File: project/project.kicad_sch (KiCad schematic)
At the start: 33 parts, among them J1 ssd1306 oled, SW1 USR_BTN, T1 xh3p, T2 xh3p, T3 xh3p, T4 xh3p, T5 xh3p, T6 xh3p, T7 xh3p, T8 xh3p, U1 esp32-c3-supermini

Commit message: everything has changed
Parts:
- removed R15: 330, Resistor_SMD:R_0805_2012Metric, symbol Device:R
- removed R16: 4k7, Resistor_SMD:R_0805_2012Metric, symbol Device:R
- removed T1, T2, T3, T4, T5, T6, T7, T8: xh3p, -local:JST_XH_S3B-XH-SM4-TB_1x03-1MP_P2.50mm_Horizontal, symbol Connector_Generic_MountingPin:Conn_01x03_MountingPin
- added C1: 10u, Capacitor_SMD:C_0805_2012Metric_Pad1.18x1.45mm_HandSolder, symbol Device:C
- added D2: LED, LED_SMD:LED_0805_2012Metric_Pad1.15x1.40mm_HandSolder, symbol Device:LED
- added R18, R21, R22, R3: 330, Resistor_SMD:R_0805_2012Metric, symbol Device:R
- added R19, R2, R20: 4k7, Resistor_SMD:R_0805_2012Metric, symbol Device:R
- added SW1: USR_BTN, Button_Switch_SMD:SW_SPST_PTS645, symbol Switch:SW_Push
- added T1, T2, T3, T4, T5, T6, T7, T8: PJ-242, -local:PJ-242, symbol Connector:AudioJack4_SwitchTR1
- J1: footprint -local:oled_i2c_128x32_ssd1306 -> -local:oled_i2c_128x64_ssd1306
- R1, R10, R11, R12, R13, R14, R17, R4, R5, R6, R7, R8, R9: lcsc# C17414 -> (none)
- R15: renamed from R3; lcsc# C17414 -> (none)
- R16: renamed from R2; lcsc# C17414 -> (none)
- renumbered C1 to C2, SW1 to SW2
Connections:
- net +3V3: now also R1.2, R10.2, R11.2, R12.2, R13.2, R14.2, R15.2, R16.2, R4.2, R5.2, R6.2, R7.2, R8.2, R9.2, C1.1, R19.2, R2.2, R20.2, R3.2; no longer R10.1, R11.1, R12.1, R13.1, R14.1, R15.1, R16.1, R17.1, R4.1, R5.1, R6.1, R7.1, R8.1, R9.1
- net GND: now also C1.2, D2.1 (K), SW1.2, T1.R2, T2.R2, T3.R2, T4.R2, T5.R2, T6.R2, T7.R2, T8.R2
- net LED: now also R17.2, R18.2; no longer R1.1
- net SCL: now also R20.1
- net SDA: now also R19.1
- net T1: now also U1.13 (IO4/ADC1_4/SPI_SCK), R2.1, T1.T; no longer R16.2, U1.1 (IO5/ADC2/SPI_MISO)
- net T2: now also R4.1, U1.12 (IO3/ADC1_3), T2.T; no longer R4.2, U1.6 (IO10)
- net T3: now also R6.1, U1.10 (IO1/ADC1_1), T3.T; no longer R6.2, U1.2 (IO6/SPI_MOSI)
- net T4: now also R8.1, U1.9 (IO0/ADC1_0), T4.T; no longer R8.2, U1.3 (IO7/SPI_SS)
- net T5: now also R10.1, U1.1 (IO5/ADC2/SPI_MISO), T5.T; no longer R10.2, U1.12 (IO3/ADC1_3)
- net T6: now also R12.1, U1.2 (IO6/SPI_MOSI), T6.T; no longer R12.2, U1.10 (IO1/ADC1_1)
- net T7: now also R14.1, U1.3 (IO7/SPI_SS), T7.T; no longer R14.2, U1.9 (IO0/ADC1_0)
- net T8: now also R16.1, U1.6 (IO10), T8.T; no longer U1.13 (IO4/ADC1_4/SPI_SCK)
- net BTN2: now reaches U1.8 (IO21/TX)
- net BTN2: now also R22.1
- net at D1.1 (K): now also R17.1; no longer R1.2
- net BTN: no longer names the net of SW2.1
- net BTN: now also R22.2; no longer U1.11 (IO2/ADC1_2/BOOT)
- new net: R3.1, T2.S
- new net: R1.1, T1.S
- new net: R13.1, T7.S
- new net: R9.1, T5.S
- new net: D2.2 (A), R18.1
- new net: R21.2, SW1.1
- new net: R5.1, T3.S
- new net: R7.1, T4.S
- new net: R15.1, T8.S
- new net: R11.1, T6.S
- new net BTN1: R21.1, U1.11 (IO2/ADC1_2/BOOT)
- no-connect marks 1 -> 24
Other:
- moved on the sheet: C2, D1, J1, R15, R16, SW2, U1

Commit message: updating bom and pnp positions
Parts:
- C1, C2: jlc-part-type (none) -> B; lcsc# (none) -> C15850
- D1: value LED -> LED-R; jlc-part-type (none) -> B; lcsc# (none) -> C84256
- D2: value LED -> LED-G; jlc-part-type (none) -> B; lcsc# (none) -> C2297
- H1, J1, U1: jlc-part-type (none) -> -
- R1, R11, R13, R15, R17, R18, R21, R22, R3, R5, R7, R9: lcsc# (none) -> C17630
- R10, R12, R14, R16, R19, R2, R20, R4, R6, R8: lcsc# (none) -> C17673
- SW1, SW2: jlc-part-type (none) -> E; lcsc# (none) -> C2689405
- T1, T2, T3, T4, T5, T6, T7, T8: jlc-part-type (none) -> E

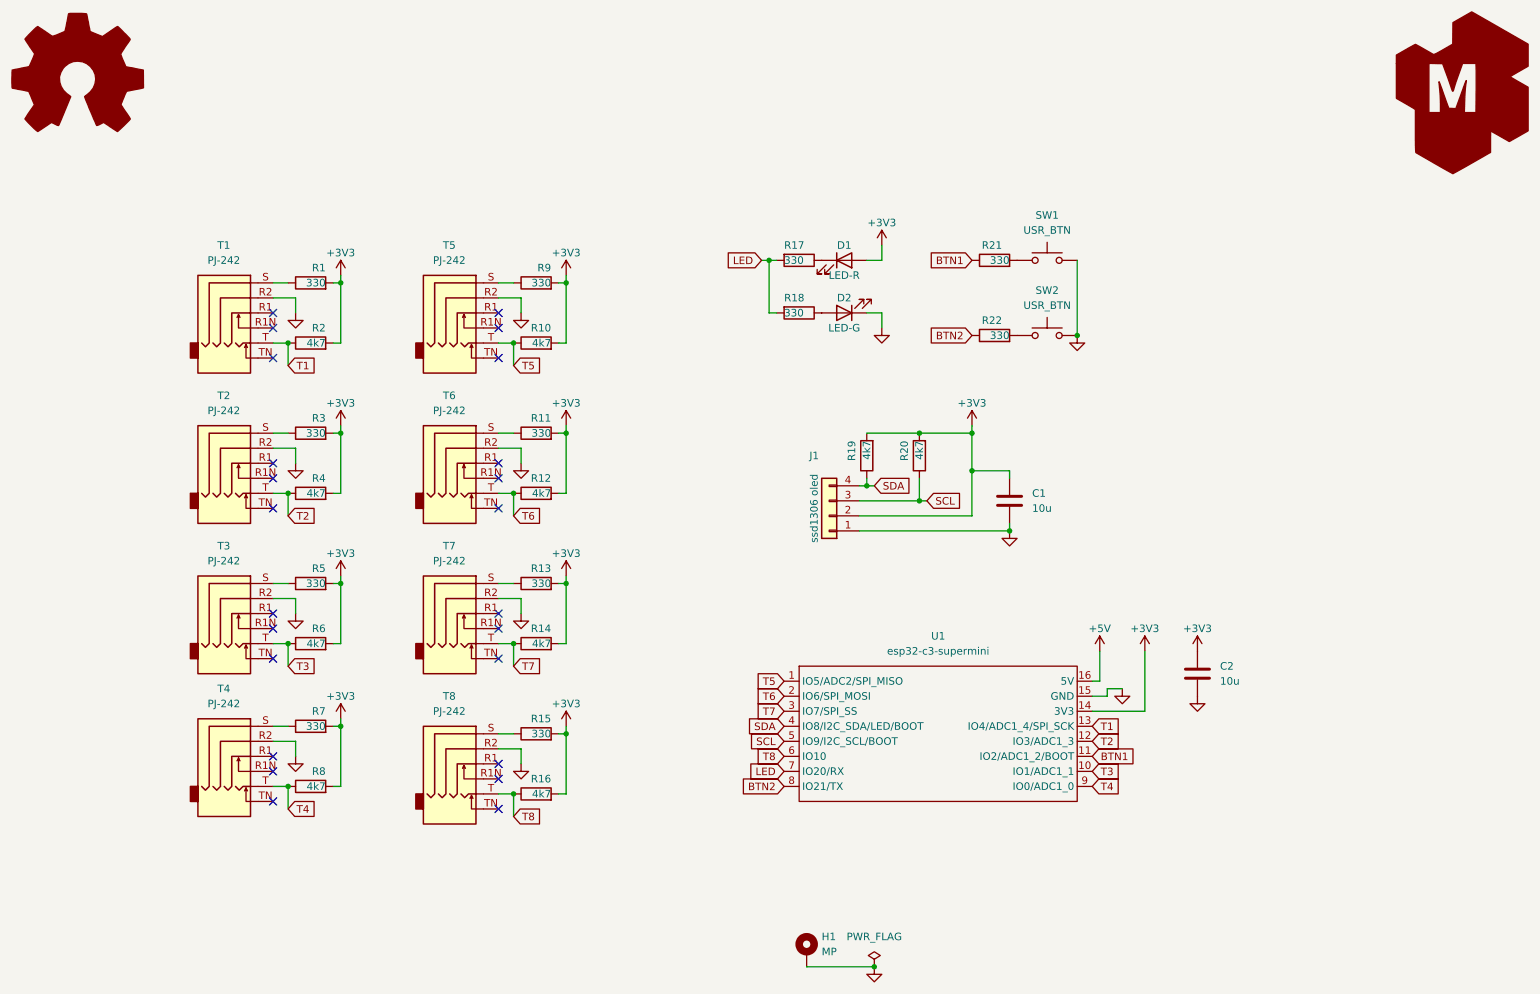
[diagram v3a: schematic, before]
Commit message: fixed bugs from v1.0
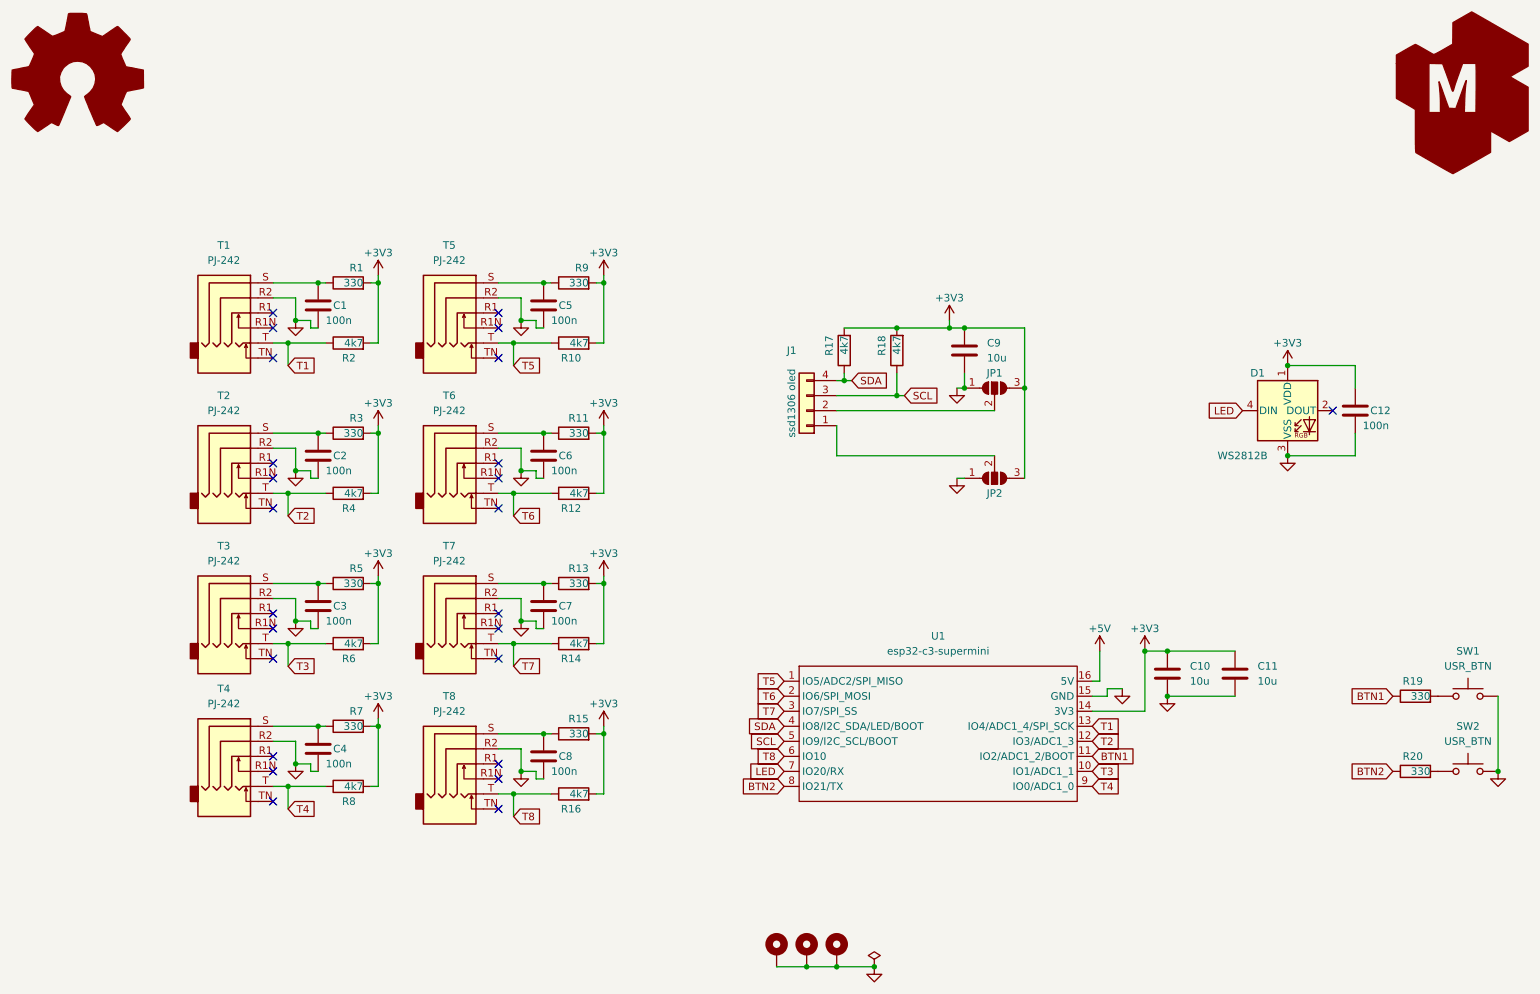
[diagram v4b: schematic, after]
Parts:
- removed D1: LED-R, LED_SMD:LED_0805_2012Metric_Pad1.15x1.40mm_HandSolder, symbol Device:LED
- removed D2: LED-G, LED_SMD:LED_0805_2012Metric_Pad1.15x1.40mm_HandSolder, symbol Device:LED
- removed R17, R18: 330, Resistor_SMD:R_0805_2012Metric, symbol Device:R
- added C11, C9: 10u, Capacitor_SMD:C_0805_2012Metric_Pad1.18x1.45mm_HandSolder, symbol Device:C
- added C12, C2, C3, C4, C5, C6, C7, C8: 100n, Capacitor_SMD:C_0805_2012Metric_Pad1.18x1.45mm_HandSolder, symbol Device:C
- added D1: WS2812B, LED_SMD:LED_WS2812B_PLCC4_5.0x5.0mm_P3.2mm, symbol LED:WS2812B
- added H1, H3: MP, MountingHole:MountingHole_3.2mm_M3_DIN965_Pad, symbol Mechanical:MountingHole_Pad
- added JP1: PIN2, Jumper:SolderJumper-3_P1.3mm_Open_RoundedPad1.0x1.5mm, symbol Jumper:SolderJumper_3_Open
- added JP2: PIN1, Jumper:SolderJumper-3_P1.3mm_Open_RoundedPad1.0x1.5mm, symbol Jumper:SolderJumper_3_Open
- C1: value 10u -> 100n; lcsc# C15850 -> C28233
- G1, G2: now in the parts list
- J1: footprint -local:oled_i2c_128x64_ssd1306 -> -local:oled_i2c_1.3_128x64_ssd1306
- renumbered C2 to C10, H1 to H2, R19 to R17, R20 to R18, R21 to R19, R22 to R20
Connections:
- net +3V3: now also C11.1, C12.1, C9.1, D1.1 (VDD), JP1.3 (B), JP2.3 (B); no longer C1.1, J1.2 (Pin_2)
- net GND: now also C11.2, C12.2, C2.2, C3.2, C4.2, C5.2, C6.2, C7.2, C8.2, C9.2, D1.3 (VSS), H1.1, H3.1, JP1.1 (A), JP2.1 (A); no longer J1.1 (Pin_1)
- net LED: now also D1.4 (DIN)
- net at R3.1, T2.S: now also C2.1
- net at R1.1, T1.S: now also C1.1
- net at R13.1, T7.S: now also C7.1
- net at R9.1, T5.S: now also C5.1
- net at R5.1, T3.S: now also C3.1
- net at R7.1, T4.S: now also C4.1
- net at R15.1, T8.S: now also C8.1
- net at R11.1, T6.S: now also C6.1
- new net: J1.2 (Pin_2), JP1.2 (C)
- new net: J1.1 (Pin_1), JP2.2 (C)
- no-connect marks 24 -> 25
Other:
- moved on the sheet: C10, J1, R1, R10, R11, R12, R13, R14, R15, R16, R17, R18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

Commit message: adding hard reset for sensors, removing rgb led
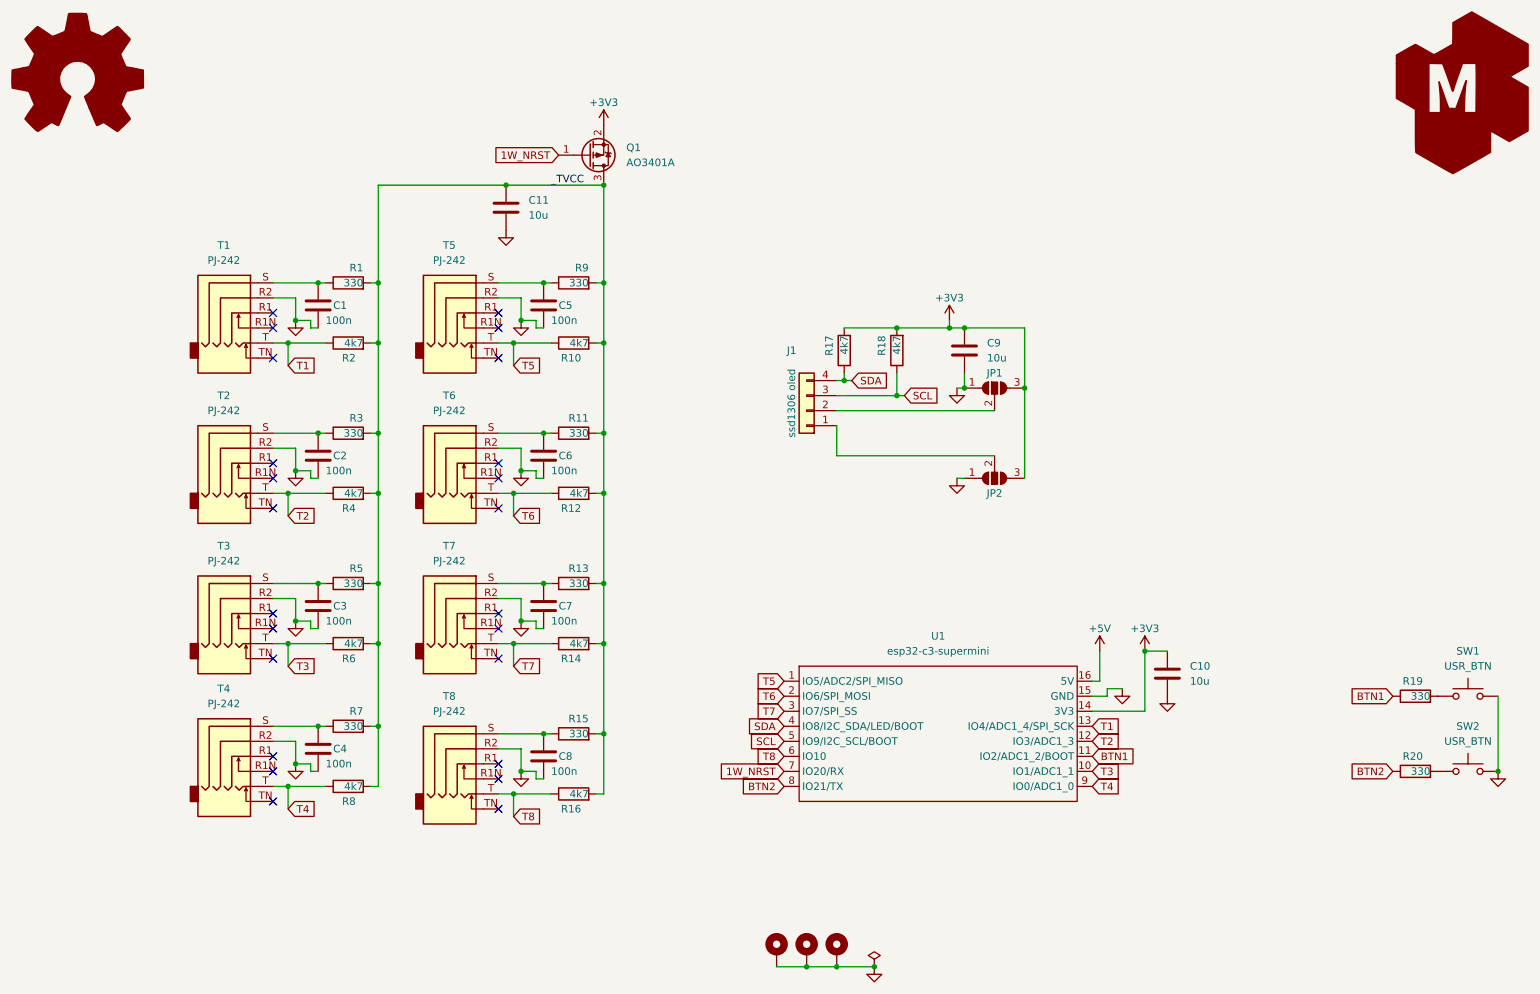
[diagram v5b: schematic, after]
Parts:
- removed C12: 100n, Capacitor_SMD:C_0805_2012Metric_Pad1.18x1.45mm_HandSolder, symbol Device:C
- removed D1: WS2812B, LED_SMD:LED_WS2812B_PLCC4_5.0x5.0mm_P3.2mm, symbol LED:WS2812B
- added Q1: AO3401A, Package_TO_SOT_SMD:SOT-23, symbol Transistor_FET:AO3401A
- G1, G2, JP1: now left out of the parts list
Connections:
- net +3V3: now also Q1.2 (S); no longer C11.1, R1.2, R10.2, R11.2, R12.2, R13.2, R14.2, R15.2, R16.2, R2.2, R3.2, R4.2, R5.2, R6.2, R7.2, R8.2, R9.2
- net LED renamed 1W_NRST
- net 1W_NRST: now also Q1.1 (G)
- new net _TVCC: C11.1, Q1.3 (D), R1.2, R10.2, R11.2, R12.2, R13.2, R14.2, R15.2, R16.2, R2.2, R3.2, R4.2, R5.2, R6.2, R7.2, R8.2, R9.2
- no-connect marks 25 -> 24
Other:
- moved on the sheet: C11

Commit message: numbering inputs, changing buttons, and adding tooling holes
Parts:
- SW1, SW2: footprint Button_Switch_SMD:SW_SPST_PTS645 -> Button_Switch_SMD:SW_SPST_TL3342; jlc-part-type E -> B; lcsc# C2689405 -> C318884
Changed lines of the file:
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@@
   (title_block
     (title "temp-1w8-pro")
-    (date "2024-12-01")
-    (rev "3.0")
+    (date "2024-12-23")
+    (rev "3.1")
     (company "makerspace.lt")
   )
@@
     (property "Reference" "SW1" (id 0) (at 265.43 127 0))
     (property "Value" "USR_BTN" (id 1) (at 265.43 129.54 0))
-    (property "Footprint" "Button_Switch_SMD:SW_SPST_PTS645" (id 2) (at 265.43 129.54 0)
-      (effects (font (size 1.27 1.27)) hide)
-    )
-    (property "Datasheet" "https://wmsc.lcsc.com/wmsc/upload/file/pdf/v2/lcsc/2102191506_DGBZ-YTSD003A0452502B_C2689405.pdf" (id 3) (at 265.43 129.54 0)
-      (effects (font (size 1.27 1.27)) hide)
-    )
-    (property "jlc-part-type" "E" (id 4) (at 265.43 134.62 0)
-      (effects (font (size 1.27 1.27)) hide)
-    )
-    (property "lcsc#" "C2689405" (id 5) (at 265.43 134.62 0)
+    (property "Footprint" "Button_Switch_SMD:SW_SPST_TL3342" (id 2) (at 265.43 129.54 0)
+      (effects (font (size 1.27 1.27)) hide)
+    )
+    (property "Datasheet" "https://jlcpcb.com/api/file/downloadByFileSystemAccessId/8550724022091735041" (id 3) (at 265.43 129.54 0)
+      (effects (font (size 1.27 1.27)) hide)
+    )
+    (property "jlc-part-type" "B" (id 4) (at 265.43 134.62 0)
+      (effects (font (size 1.27 1.27)) hide)
+    )
+    (property "lcsc#" "C318884" (id 5) (at 265.43 134.62 0)
       (effects (font (size 1.27 1.27)) hide)
     )
@@
     (property "Reference" "SW2" (id 0) (at 265.43 139.7 0))
     (property "Value" "USR_BTN" (id 1) (at 265.43 142.24 0))
-    (property "Footprint" "Button_Switch_SMD:SW_SPST_PTS645" (id 2) (at 265.43 142.24 0)
-      (effects (font (size 1.27 1.27)) hide)
-    )
-    (property "Datasheet" "https://wmsc.lcsc.com/wmsc/upload/file/pdf/v2/lcsc/2102191506_DGBZ-YTSD003A0452502B_C2689405.pdf" (id 3) (at 265.43 142.24 0)
-      (effects (font (size 1.27 1.27)) hide)
-    )
-    (property "jlc-part-type" "E" (id 4) (at 265.43 147.32 0)
-      (effects (font (size 1.27 1.27)) hide)
-    )
-    (property "lcsc#" "C2689405" (id 5) (at 265.43 147.32 0)
+    (property "Footprint" "Button_Switch_SMD:SW_SPST_TL3342" (id 2) (at 265.43 142.24 0)
+      (effects (font (size 1.27 1.27)) hide)
+    )
+    (property "Datasheet" "https://jlcpcb.com/api/file/downloadByFileSystemAccessId/8550724022091735041" (id 3) (at 265.43 142.24 0)
+      (effects (font (size 1.27 1.27)) hide)
+    )
+    (property "jlc-part-type" "B" (id 4) (at 265.43 147.32 0)
+      (effects (font (size 1.27 1.27)) hide)
+    )
+    (property "lcsc#" "C318884" (id 5) (at 265.43 147.32 0)
       (effects (font (size 1.27 1.27)) hide)
     )
@@
     )
     (path "/6c664720-d568-4a71-905b-62ee25dcbd7d"
-      (reference "SW1") (unit 1) (value "USR_BTN") (footprint "Button_Switch_SMD:SW_SPST_PTS645")
+      (reference "SW1") (unit 1) (value "USR_BTN") (footprint "Button_Switch_SMD:SW_SPST_TL3342")
     )
     (path "/d8acd61f-ad5d-4d7c-bbcb-f13a12ecbad2"
-      (reference "SW2") (unit 1) (value "USR_BTN") (footprint "Button_Switch_SMD:SW_SPST_PTS645")
+      (reference "SW2") (unit 1) (value "USR_BTN") (footprint "Button_Switch_SMD:SW_SPST_TL3342")
     )
     (path "/62dd8f70-ea37-42ca-a38e-d098658705ed"
